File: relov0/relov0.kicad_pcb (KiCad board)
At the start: 2 copper layers, 90 x 50 mm, 21 parts, among them J1 Barrel_Jack_Switch, J2 Barrel_Jack_Switch, J3 AudioJack2_SwitchT, J4 Conn_01x03_Pin, SW1 SW_SPDT, U1 NE555P, U2 L7805

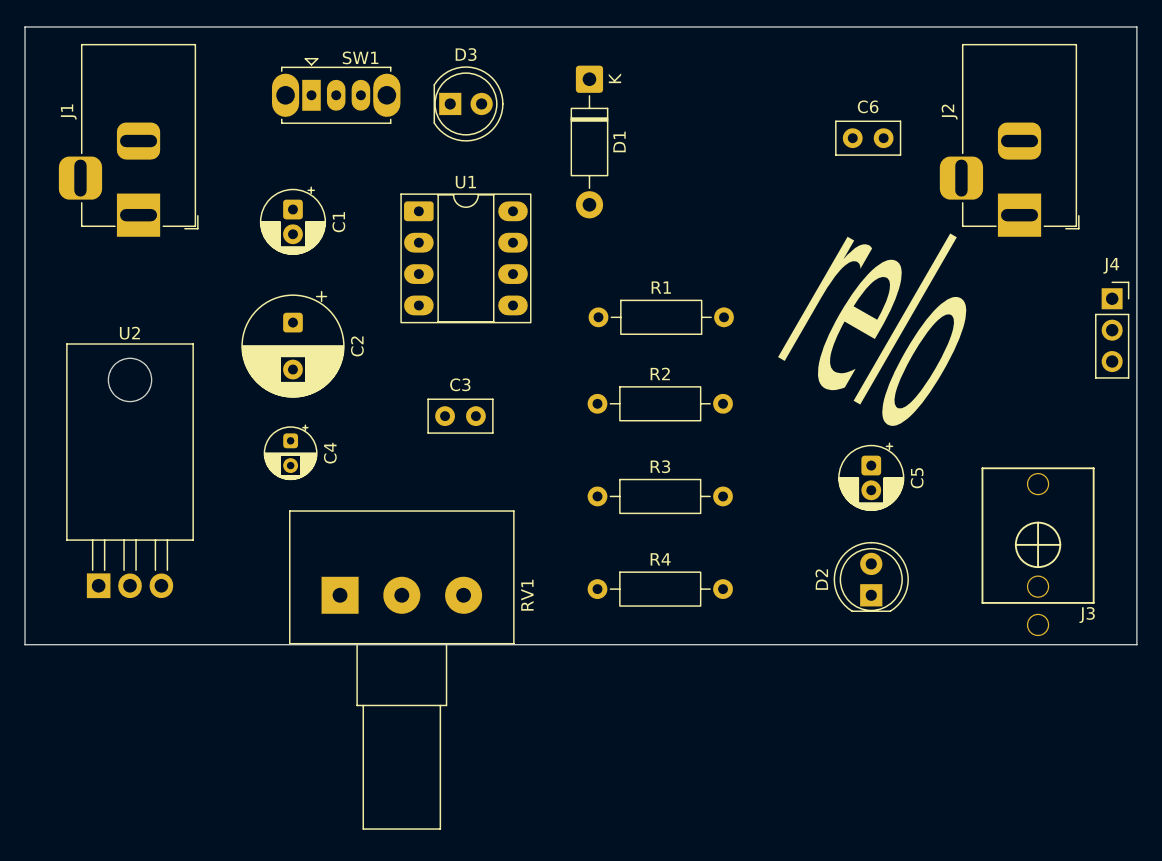
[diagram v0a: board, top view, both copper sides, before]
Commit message: agregar nuevas mods
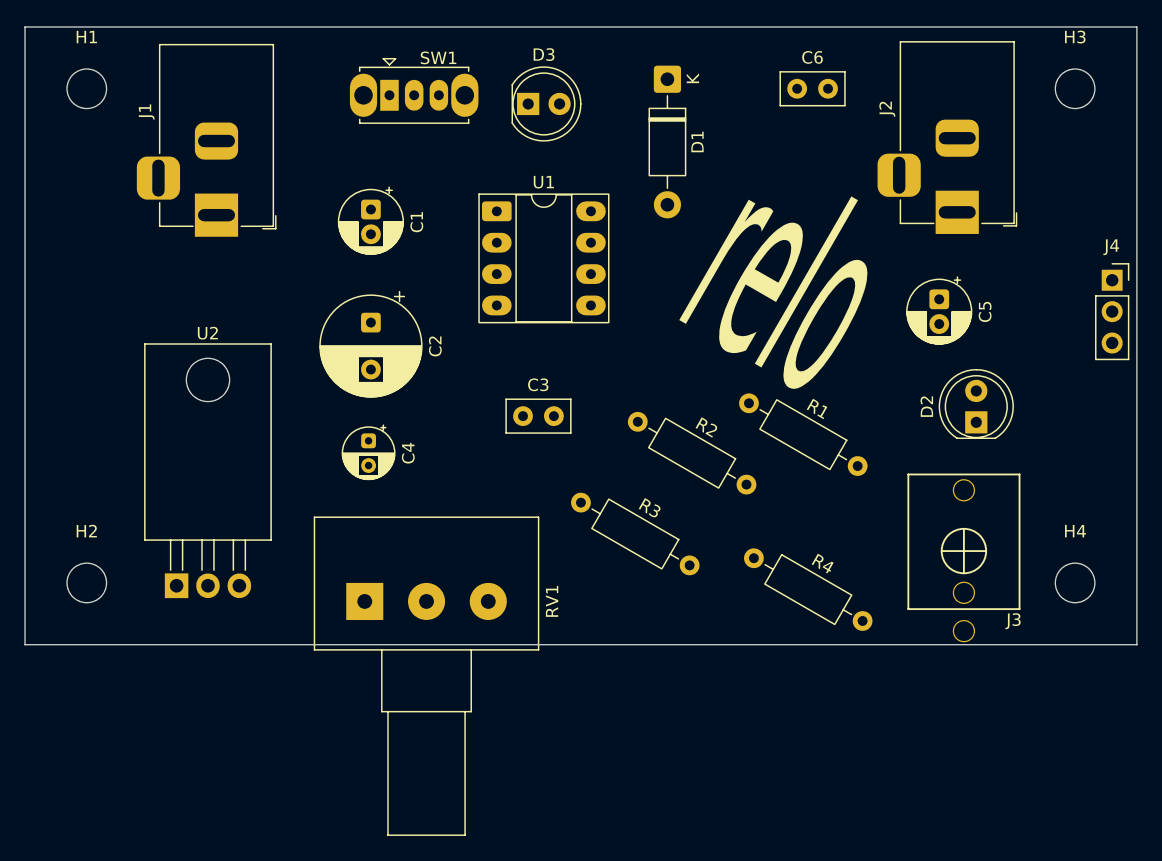
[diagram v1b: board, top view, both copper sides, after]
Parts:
- added H1: M3, MountingHole:MountingHole_3.2mm_M3, F.Cu at (55.0, 55.0)
- added H2: M3, MountingHole:MountingHole_3.2mm_M3, F.Cu at (55.0, 95.0)
- added H3: M3, MountingHole:MountingHole_3.2mm_M3, F.Cu at (135.0, 55.0)
- added H4: M3, MountingHole:MountingHole_3.2mm_M3, F.Cu at (135.0, 95.0)
- moved D2 16.4 mm to (127.0, 82.0)
- moved C5 14.5 mm to (124.0, 72.0)
- moved R1 14.0 mm to (108.6, 80.5), turned to -30 degrees
- moved R4 12.9 mm to (109.0, 93.0), turned to -30 degrees
- moved C1 6.31 mm to (78.0, 64.8)
- moved C2 6.31 mm to (78.0, 73.9)
- moved C3 6.31 mm to (90.3, 81.5)
- moved C4 6.31 mm to (77.8, 83.5)
- moved D1 6.31 mm to (102.0, 54.2)
- moved D3 6.31 mm to (90.7, 56.2)
- moved J1 6.31 mm to (65.5, 65.2)
- moved SW1 6.31 mm to (79.5, 55.5)
- moved U1 6.31 mm to (88.2, 64.9)
- moved U2 6.31 mm to (62.3, 95.2)
- moved C6 6.02 mm to (112.5, 55.0)
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
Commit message: agregar graficas
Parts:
- moved RV1 1.00 mm to (77.5, 95.5)
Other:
- board text added: "06-2026"
- board text added: "rev-a"

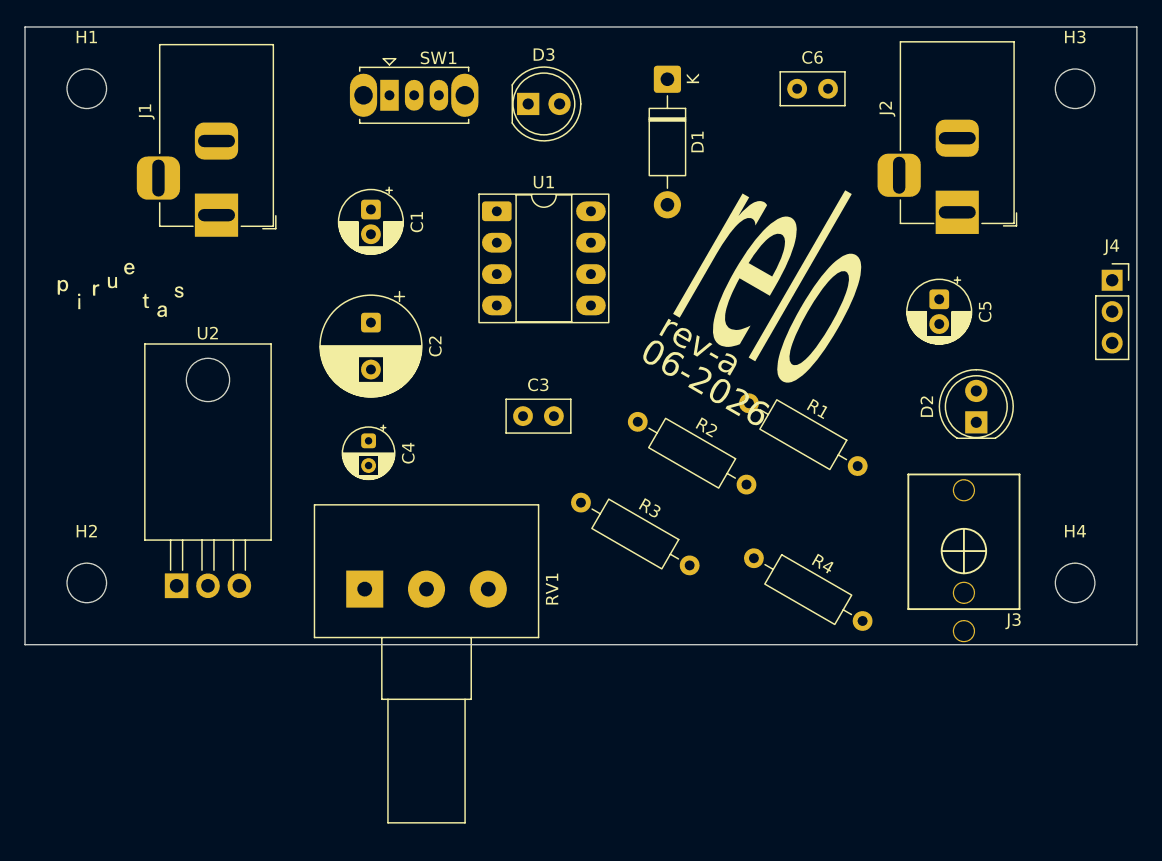
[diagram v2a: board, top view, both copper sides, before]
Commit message: agregar vias
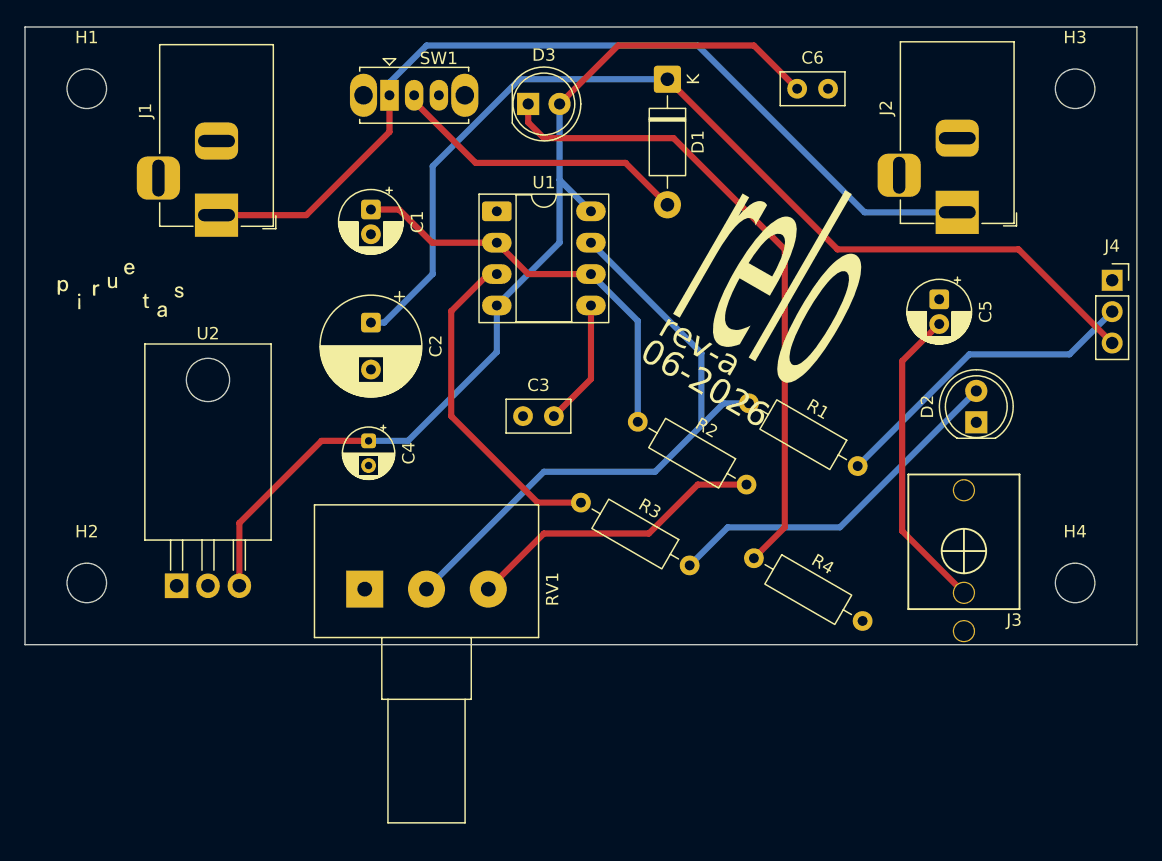
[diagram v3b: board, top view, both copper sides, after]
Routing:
- net +5V: track 0.00 -> 105.8 mm
- net +12V: track 0.00 -> 82.1 mm
- net Net-(SW1-A): track 0.00 -> 73.6 mm
- net Net-(D3-K): track 0.00 -> 52.6 mm
- net Net-(U1-DISCH): track 0.00 -> 50.8 mm
- net Net-(U1-THRES): track 0.00 -> 33.5 mm
- net Net-(D2-A): track 0.00 -> 29.0 mm
- net Net-(U1-OUT): track 0.00 -> 26.8 mm
- net Net-(C5-Pad2): track 0.00 -> 25.1 mm
- net Net-(D1-A): track 0.00 -> 25.0 mm
- net Net-(R2-Pad2): track 0.00 -> 24.4 mm
- net Net-(U1-CONT): track 0.00 -> 10.2 mm

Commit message: añadido gerb
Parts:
- C5: value 47u -> 220u
- SW1: footprint Button_Switch_THT:SW_Slide_SPDT_Straight_CK_OS102011MS2Q -> dis8644:spdt_ssd12d00g3
- moved J3 1.42 mm to (126.0, 91.0)
- turned SW1 to 180 degrees
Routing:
- net Net-(U1-OUT): track 26.8 -> 62.6 mm, vias 0 -> 2
- net +5V: track 105.8 -> 140.3 mm
- net +12V: track 82.1 -> 111.1 mm
- net Net-(D1-A): track 25.0 -> 33.3 mm
- net Net-(C5-Pad2): track 25.1 -> 24.5 mm
- added copper zone on B.Cu, net GND
- added copper zone on F.Cu, net GND
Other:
- board text added: "ON"
